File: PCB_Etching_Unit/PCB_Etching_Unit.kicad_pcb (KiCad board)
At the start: 2 copper layers, 61 parts, among them M1 Motor_DC, M2 Motor_DC, Q1 TIP42, Q10 TIP42, Q11 TIP41, Q12 2N3904, Q13 TIP42, Q2 TIP42, Q3 TIP42, Q4 TIP42, Q5 TIP42, Q6 TIP41, Q7 TIP41, Q8 TIP42, Q9 TIP41, SW1 SW_MEC_5G, SW2 SW_MEC_5G, SW4 SW_MEC_5G, SW5 SW_MEC_5G, SW6 SW_MEC_5G, U1 HDSP-7801, U10 4011, U2 HDSP-7801, U3 HDSP-7801, U4 HDSP-7801, U5 4027, U7 4027, U8 4027, U9 4011

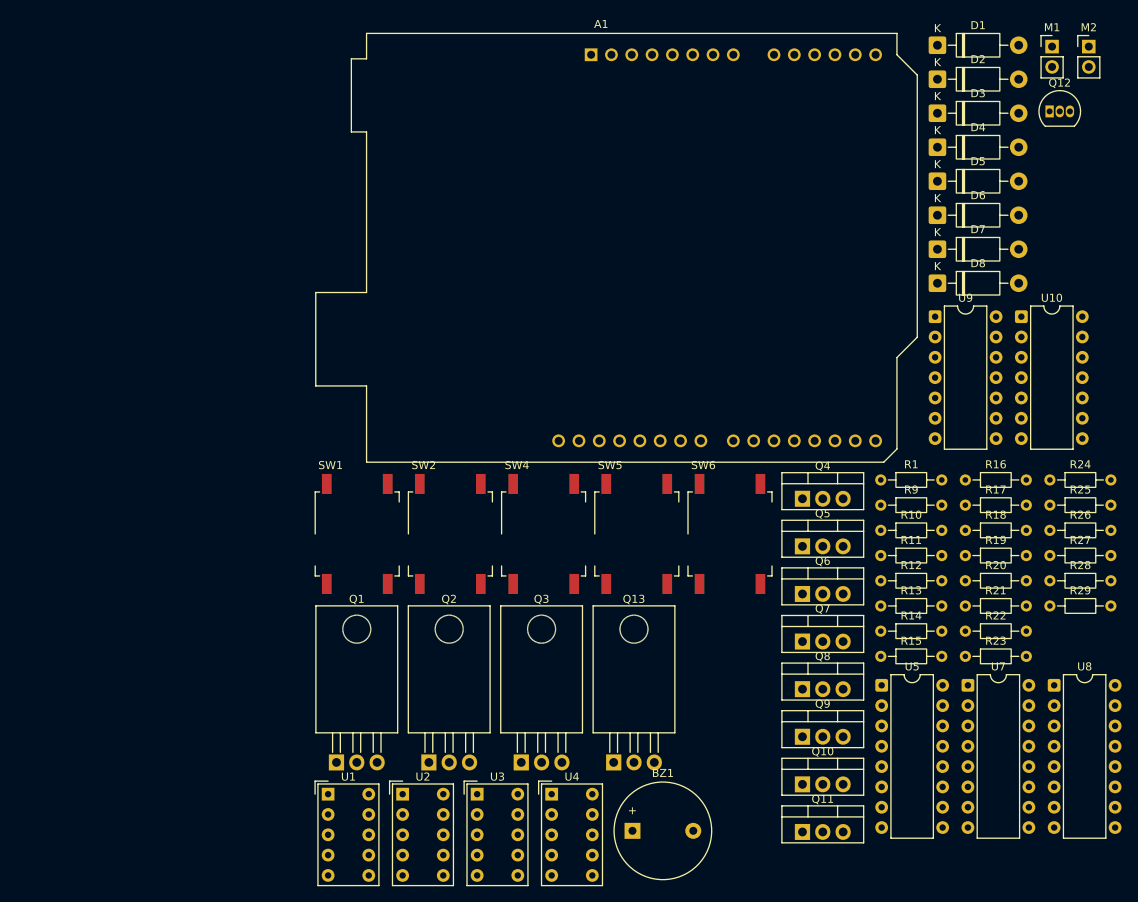
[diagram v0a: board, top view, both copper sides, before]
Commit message: Added poti for speed control and manual mode button.
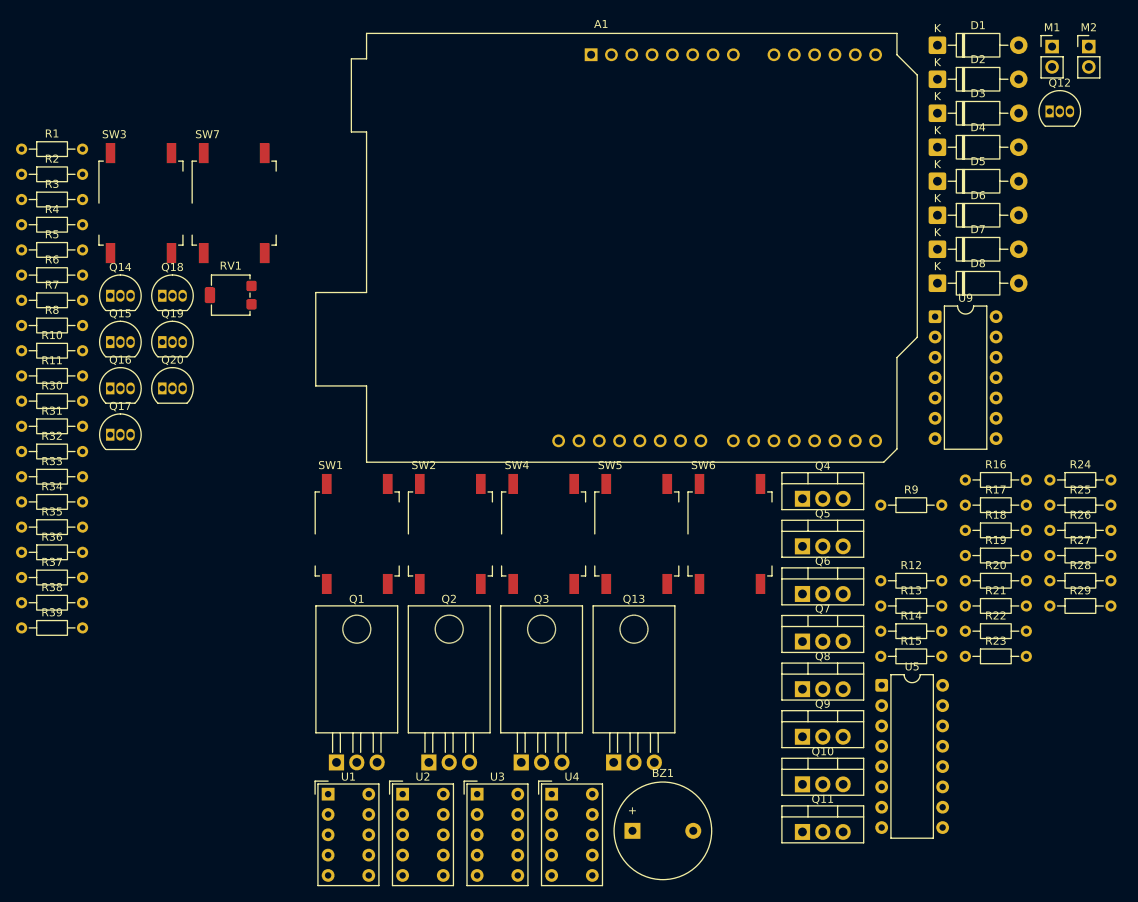
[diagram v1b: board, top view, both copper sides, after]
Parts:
- removed U10: 4011, Package_DIP:DIP-14_W7.62mm
- removed U7, U8: 4027, Package_DIP:DIP-16_W7.62mm
- added Q14: BC550, Package_TO_SOT_THT:TO-92_Inline, F.Cu at (87.1, 72.6)
- added Q15: BC550, Package_TO_SOT_THT:TO-92_Inline, F.Cu at (87.1, 78.4)
- added Q16: BC550, Package_TO_SOT_THT:TO-92_Inline, F.Cu at (87.1, 84.2)
- added Q17: BC550, Package_TO_SOT_THT:TO-92_Inline, F.Cu at (87.1, 90.0)
- added Q18: BC550, Package_TO_SOT_THT:TO-92_Inline, F.Cu at (93.6, 72.6)
- added Q19: BC550, Package_TO_SOT_THT:TO-92_Inline, F.Cu at (93.6, 78.4)
- added Q20: BC550, Package_TO_SOT_THT:TO-92_Inline, F.Cu at (93.6, 84.2)
- added R2: 1K, Resistor_THT:R_Axial_DIN0204_L3.6mm_D1.6mm_P7.62mm_Horizontal, F.Cu at (76.0, 57.4)
- added R3: 2.2K, Resistor_THT:R_Axial_DIN0204_L3.6mm_D1.6mm_P7.62mm_Horizontal, F.Cu at (76.0, 60.6)
- added R30: 1K, Resistor_THT:R_Axial_DIN0204_L3.6mm_D1.6mm_P7.62mm_Horizontal, F.Cu at (76.0, 85.8)
- added R31: 2.2K, Resistor_THT:R_Axial_DIN0204_L3.6mm_D1.6mm_P7.62mm_Horizontal, F.Cu at (76.0, 88.9)
- added R32: 1K, Resistor_THT:R_Axial_DIN0204_L3.6mm_D1.6mm_P7.62mm_Horizontal, F.Cu at (76.0, 92.1)
- added R33: 2.2K, Resistor_THT:R_Axial_DIN0204_L3.6mm_D1.6mm_P7.62mm_Horizontal, F.Cu at (76.0, 95.2)
- added R34: 1K, Resistor_THT:R_Axial_DIN0204_L3.6mm_D1.6mm_P7.62mm_Horizontal, F.Cu at (76.0, 98.4)
- added R35: 2.2K, Resistor_THT:R_Axial_DIN0204_L3.6mm_D1.6mm_P7.62mm_Horizontal, F.Cu at (76.0, 101.5)
- added R36: 1K, Resistor_THT:R_Axial_DIN0204_L3.6mm_D1.6mm_P7.62mm_Horizontal, F.Cu at (76.0, 104.7)
- added R37: 6.8K, Resistor_THT:R_Axial_DIN0204_L3.6mm_D1.6mm_P7.62mm_Horizontal, F.Cu at (76.0, 107.8)
- added R38: 15K, Resistor_THT:R_Axial_DIN0204_L3.6mm_D1.6mm_P7.62mm_Horizontal, F.Cu at (76.0, 111.0)
- added R39: 1K, Resistor_THT:R_Axial_DIN0204_L3.6mm_D1.6mm_P7.62mm_Horizontal, F.Cu at (76.0, 114.1)
- added R4: 1K, Resistor_THT:R_Axial_DIN0204_L3.6mm_D1.6mm_P7.62mm_Horizontal, F.Cu at (76.0, 63.7)
- added R5: 1K, Resistor_THT:R_Axial_DIN0204_L3.6mm_D1.6mm_P7.62mm_Horizontal, F.Cu at (76.0, 66.9)
- added R6: 2.2K, Resistor_THT:R_Axial_DIN0204_L3.6mm_D1.6mm_P7.62mm_Horizontal, F.Cu at (76.0, 70.0)
- added R7: 1K, Resistor_THT:R_Axial_DIN0204_L3.6mm_D1.6mm_P7.62mm_Horizontal, F.Cu at (76.0, 73.2)
- added R8: 2.2K, Resistor_THT:R_Axial_DIN0204_L3.6mm_D1.6mm_P7.62mm_Horizontal, F.Cu at (76.0, 76.3)
- added RV1: 50K, Potentiometer_SMD:Potentiometer_Bourns_3214G_Horizontal, F.Cu at (102.2, 72.5)
- added SW3: SW_MEC_5G, Button_Switch_SMD:SW_MEC_5GSH9, F.Cu at (91.0, 61.0)
- added SW7: SW_MEC_5G, Button_Switch_SMD:SW_MEC_5GSH9, F.Cu at (102.6, 61.0)
- R11: value 1K -> 2.2K
- moved R1 115.1 mm to (76.0, 54.3)
- moved R10 109.7 mm to (76.0, 79.5)
- moved R11 109.7 mm to (76.0, 82.6)
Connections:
- A1 pad 10: Net-(A1-A1) -> /UP
- A1 pad 11: Net-(A1-A2) -> unconnected-(A1-A2-Pad11)
- A1 pad 19: unconnected-(A1-D4-Pad19) -> Net-(A1-D4)
- A1 pad 20: unconnected-(A1-D5-Pad20) -> Net-(A1-D5)
- A1 pad 21: unconnected-(A1-D6-Pad21) -> Net-(A1-D6)
- A1 pad 22: unconnected-(A1-D7-Pad22) -> Net-(A1-D7)
- A1 pad 23: unconnected-(A1-D8-Pad23) -> Net-(A1-D8)
- A1 pad 24: unconnected-(A1-D9-Pad24) -> Net-(A1-D9)
- A1 pad 27: Net-(A1-D12) -> unconnected-(A1-D12-Pad27)
- A1 pad 28: Net-(A1-D13) -> unconnected-(A1-D13-Pad28)
- A1 pad 9: /UP -> Net-(A1-A0)
- R1 pad 1: Net-(Q13-B) -> Net-(Q1-B)
- R1 pad 2: Net-(A1-D13) -> Net-(A1-D7)
- R10 pad 1: Net-(A1-D11) -> Net-(Q16-B)
- R10 pad 2: Net-(Q2-B) -> Net-(U11-Qc)
- R11 pad 1: Net-(Q1-B) -> VCC
- R11 pad 2: Net-(A1-D12) -> Net-(Q17-C)
- R12 pad 1: unconnected-(R12-Pad1) -> Net-(Q12-B)
- R12 pad 2: Net-(Q12-B) -> Net-(A1-D0/RX)
- R13 pad 1: /SAVE -> /START
- R13 pad 2: /ALARM-STOP -> /SAVE
- R14 pad 1: /ALARM-STOP -> /SAVE
- R14 pad 2: /ALARM-SLEEP -> /ALARM-STOP
- R19 pad 2: Net-(A1-A1) -> Net-(A1-D11)
- R20 pad 2: Net-(A1-A2) -> Net-(A1-D10)
- R21 pad 2: Net-(A1-A1) -> Net-(A1-D11)
- R26 pad 2: Net-(A1-A2) -> Net-(A1-D10)
- R29 pad 1: /SAVE -> /START
- R9 pad 1: Net-(A1-D10) -> Net-(Q13-B)
- R9 pad 2: Net-(Q3-B) -> Net-(A1-D6)
- SW1 pad 1: /ALARM-STOP -> /SAVE
- SW1 pad 2: /ALARM-STOP -> /SAVE
- SW2 pad 1: /ALARM-SLEEP -> /ALARM-STOP
- SW2 pad 2: /ALARM-SLEEP -> /ALARM-STOP
- SW6 pad 1: /SAVE -> /START
- SW6 pad 2: /SAVE -> /START
- U1 pad 1: Net-(Q1-C) -> Net-(Q2-C)
- U1 pad 10: unconnected-(U1-A-Pad10) -> Net-(Q14-E)
- U1 pad 2: unconnected-(U1-F-Pad2) -> Net-(Q19-E)
- U1 pad 3: unconnected-(U1-G-Pad3) -> Net-(Q20-E)
- U1 pad 4: unconnected-(U1-E-Pad4) -> Net-(Q18-E)
- U1 pad 5: unconnected-(U1-D-Pad5) -> Net-(Q17-E)
- U1 pad 6: Net-(Q1-C) -> Net-(Q2-C)
- U1 pad 7: unconnected-(U1-DP-Pad7) -> GND
- U1 pad 8: unconnected-(U1-C-Pad8) -> Net-(Q16-E)
- U1 pad 9: unconnected-(U1-B-Pad9) -> Net-(Q15-E)
- U2 pad 1: Net-(Q2-C) -> Net-(Q1-C)
- U2 pad 10: unconnected-(U2-A-Pad10) -> Net-(Q14-E)
- U2 pad 2: unconnected-(U2-F-Pad2) -> Net-(Q19-E)
- U2 pad 3: unconnected-(U2-G-Pad3) -> Net-(Q20-E)
- U2 pad 4: unconnected-(U2-E-Pad4) -> Net-(Q18-E)
- U2 pad 5: unconnected-(U2-D-Pad5) -> Net-(Q17-E)
- U2 pad 6: Net-(Q2-C) -> Net-(Q1-C)
- U2 pad 7: unconnected-(U2-DP-Pad7) -> GND
- U2 pad 8: unconnected-(U2-C-Pad8) -> Net-(Q16-E)
- U2 pad 9: unconnected-(U2-B-Pad9) -> Net-(Q15-E)
- U3 pad 1: Net-(Q3-C) -> Net-(Q13-C)
- U3 pad 10: unconnected-(U3-A-Pad10) -> Net-(Q14-E)
- U3 pad 2: unconnected-(U3-F-Pad2) -> Net-(Q19-E)
- U3 pad 3: unconnected-(U3-G-Pad3) -> Net-(Q20-E)
- U3 pad 4: unconnected-(U3-E-Pad4) -> Net-(Q18-E)
- U3 pad 5: unconnected-(U3-D-Pad5) -> Net-(Q17-E)
- U3 pad 6: Net-(Q3-C) -> Net-(Q13-C)
- U3 pad 7: unconnected-(U3-DP-Pad7) -> GND
- U3 pad 8: unconnected-(U3-C-Pad8) -> Net-(Q16-E)
- U3 pad 9: unconnected-(U3-B-Pad9) -> Net-(Q15-E)
- U4 pad 1: Net-(Q13-C) -> Net-(Q3-C)
- U4 pad 10: unconnected-(U4-A-Pad10) -> Net-(Q14-E)
- U4 pad 2: unconnected-(U4-F-Pad2) -> Net-(Q19-E)
- U4 pad 3: unconnected-(U4-G-Pad3) -> Net-(Q20-E)
- U4 pad 4: unconnected-(U4-E-Pad4) -> Net-(Q18-E)
- U4 pad 5: unconnected-(U4-D-Pad5) -> Net-(Q17-E)
- U4 pad 6: Net-(Q13-C) -> Net-(Q3-C)
- U4 pad 7: unconnected-(U4-DP-Pad7) -> GND
- U4 pad 8: unconnected-(U4-C-Pad8) -> Net-(Q16-E)
- U4 pad 9: unconnected-(U4-B-Pad9) -> Net-(Q15-E)
- U5 pad 1: Net-(U5A-Q) -> unconnected-(U5A-Q-Pad1)
- U5 pad 12: Net-(U5A-R) -> unconnected-(U5B-R-Pad12)
- U5 pad 15: Net-(U5A-J) -> Net-(U5A-C)
- U5 pad 3: unconnected-(U5A-C-Pad3) -> Net-(U5A-C)
- U5 pad 4: Net-(U5A-R) -> unconnected-(U5A-R-Pad4)
- U5 pad 6: Net-(U5A-J) -> Net-(U5A-C)
- U9 pad 1: Net-(A1-D0/RX) -> Net-(A1-D1/TX)
- U9 pad 12: Net-(U5A-J) -> Net-(U5A-C)
- U9 pad 13: Net-(U5A-J) -> Net-(U5A-C)
- U9 pad 2: Net-(A1-D0/RX) -> Net-(A1-D1/TX)
- U9 pad 3: Net-(U6B-K) -> unconnected-(U9-Pad3)
